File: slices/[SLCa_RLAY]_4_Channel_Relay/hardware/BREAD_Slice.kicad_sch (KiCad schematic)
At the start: 38 parts, among them J1 Conn_01x10_Female, J2 Screw_Terminal_01x03, J3 Screw_Terminal_01x03, J4 Screw_Terminal_01x03, J5 Screw_Terminal_01x03, J6 Screw_Terminal_01x04, K1 G5Q-1, K2 G5Q-1, K3 G5Q-1, K4 G5Q-1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

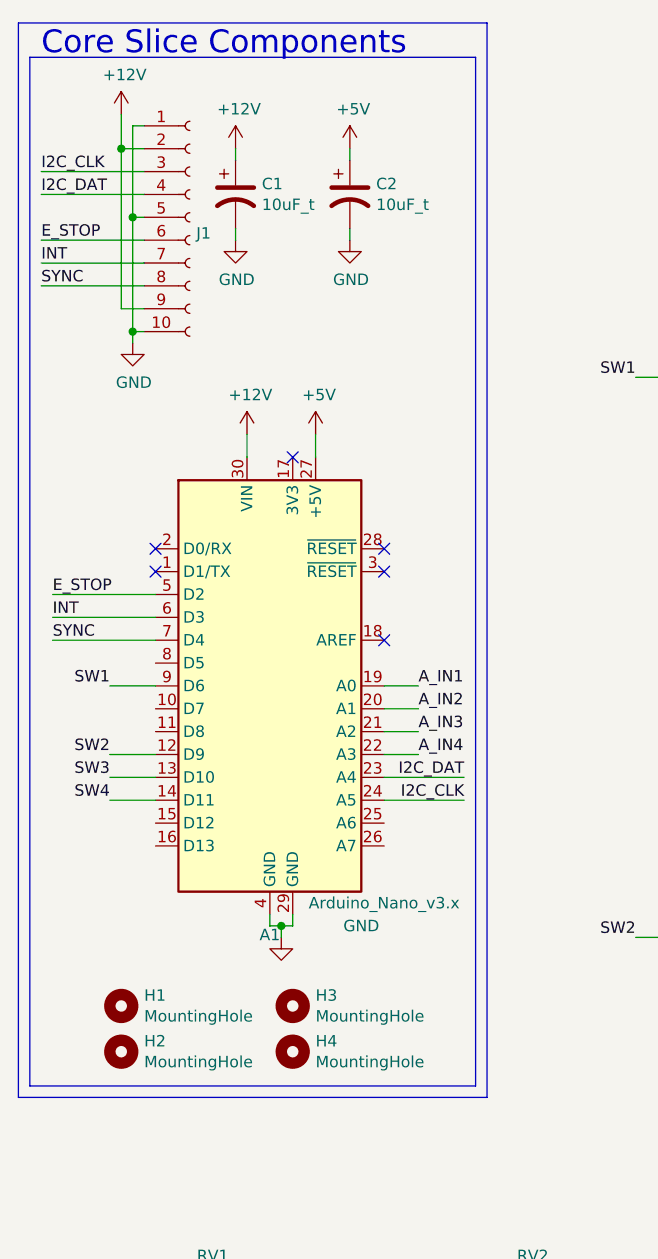
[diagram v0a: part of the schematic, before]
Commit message: restructuring for rpi boards
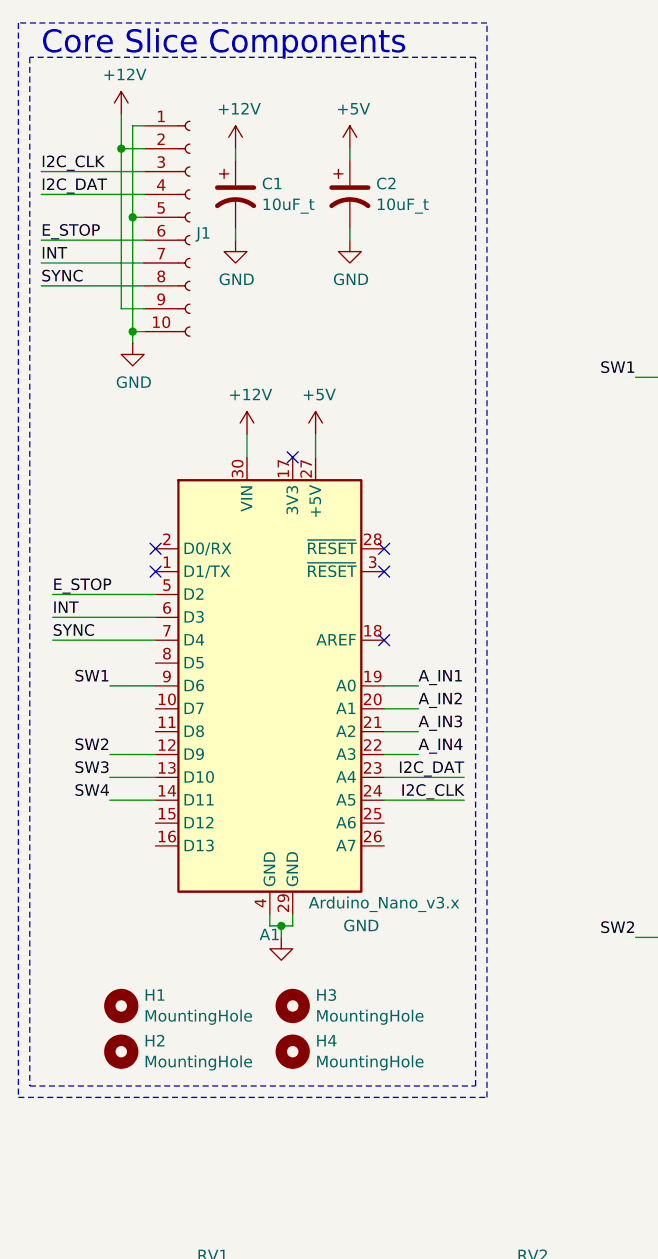
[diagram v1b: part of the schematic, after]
